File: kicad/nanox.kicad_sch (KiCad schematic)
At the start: 137 parts, among them P1 likely an ESD protection diod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, P2 likely an ESD protection diod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, P3 likely an ESD protection diod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, P4 likely an ESD protection diod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, P5 likely an ESD protection diod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, SW1 push button, left, SW2 push button, right, X1 ?, X10 unknown, marked 1C4F, likely 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, X2 unknown, marked 2GC, X3 unknown, marked 6, X4 ?, X5 ?, X6 ?, X7 ?, X8 ?, X9 unknown, marked P8W 26, Y1 crystal, likely the 32 MHz HSE

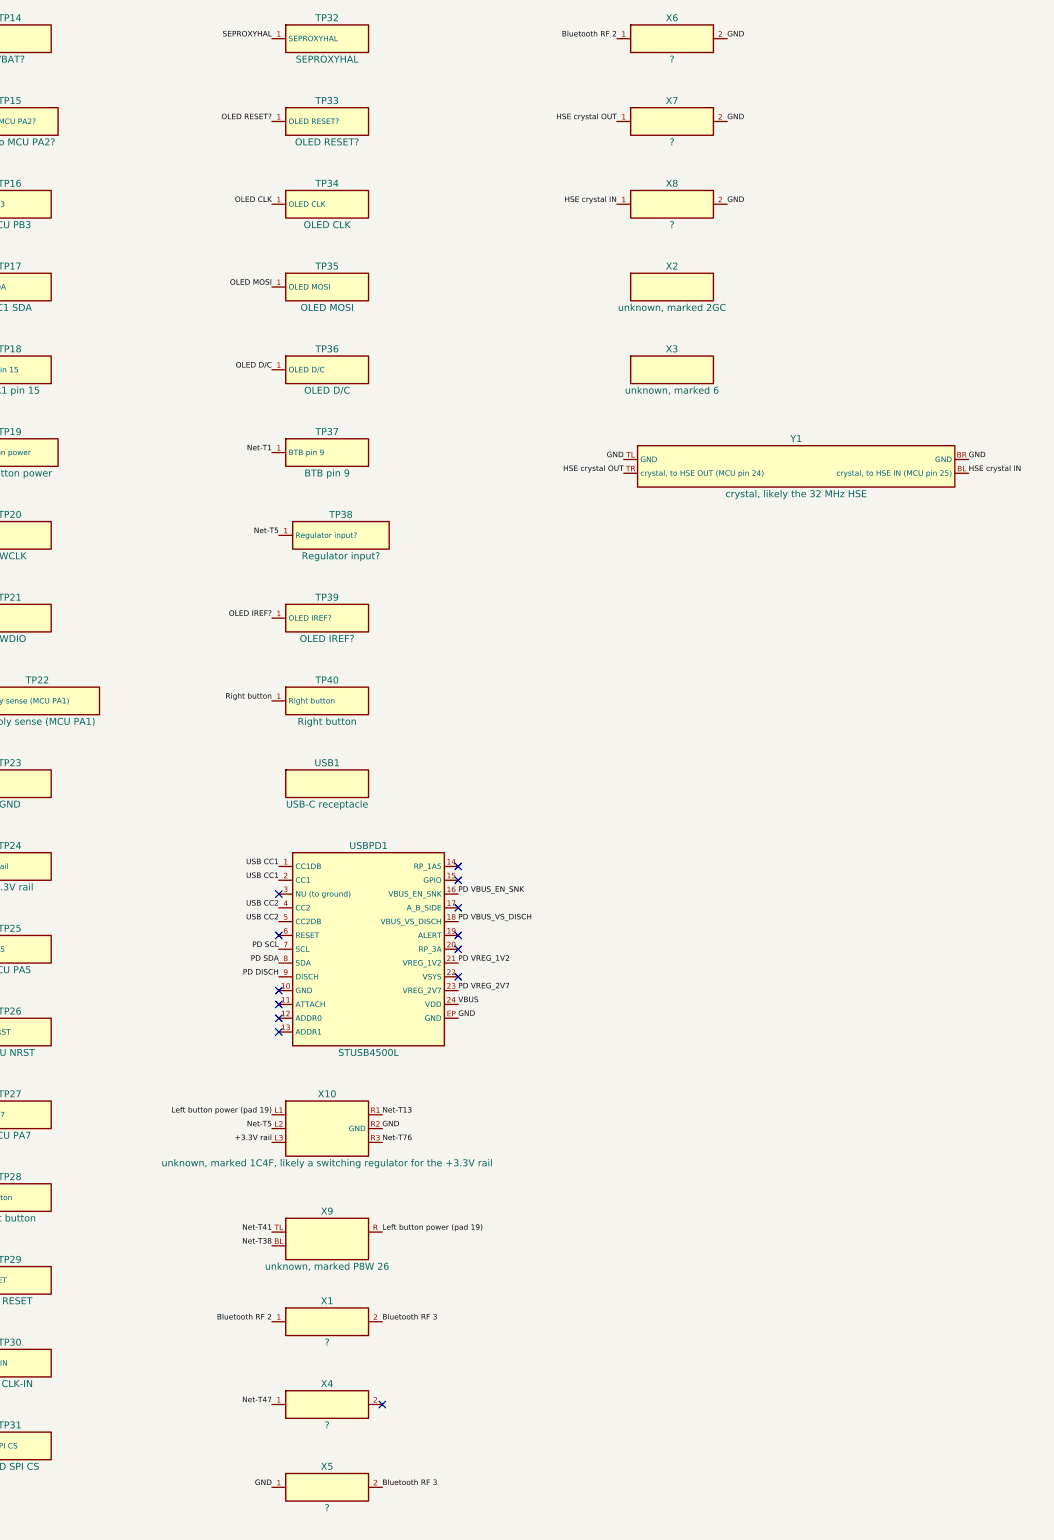
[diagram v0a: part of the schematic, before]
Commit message: Give USB1 its real pins: 24 USB-C contacts and 4 shell tabs
USB1 was a single body pad. It now has the 24 pads measured in the bare
front photo, in two staggered rows at 0.5 mm pitch (B1-B12 nearer the
mouth, A12-A1 behind), named from the USB-C pinout, plus the four shell
tabs. The traced lines land on VBUS (A4, A9, B4, B9), CC1, CC2, D+ (A6,
B6) and D- (A7, B7); the USB 3 pairs and SBU are unused. The 3D model's
solder tails now sit on the A row.

Co-Authored-By: Claude Opus 5.5 <noreply@anthropic.com>
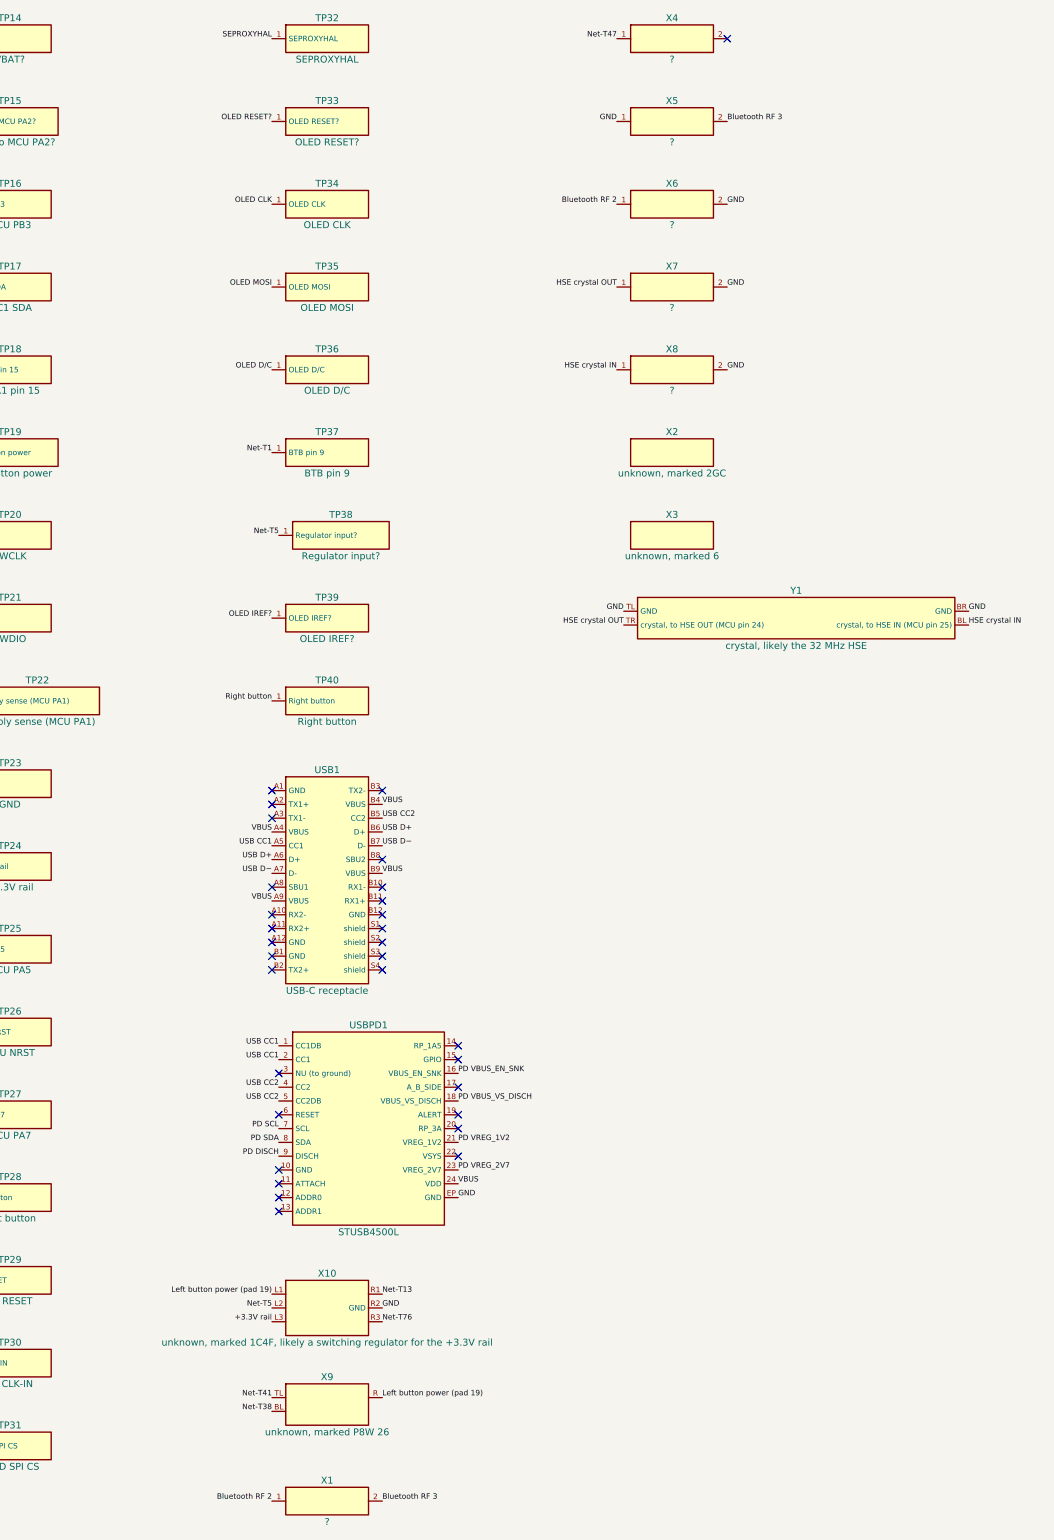
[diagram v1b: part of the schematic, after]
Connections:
- net USB CC1: now also USB1.A5 (CC1)
- net USB CC2: now also USB1.B5 (CC2)
- net USB D+: now also USB1.A6 (D+), USB1.B6 (D+)
- net USB D−: now also USB1.A7 (D-), USB1.B7 (D-)
- net VBUS: now also USB1.A4 (VBUS), USB1.A9 (VBUS), USB1.B4 (VBUS), USB1.B9 (VBUS)
- no-connect marks 61 -> 79
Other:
- moved on the sheet: USBPD1, X1, X10, X2, X3, X4, X5, X6, X7, X8, X9, Y1

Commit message: Name the display connector's power pins from the SSD1312 datasheet
The display's controller is an SSD1312, whose datasheet explains the
pins we could only guess:
- pin 12 (pad 38) is the panel's drive supply VCC, 7.5 to 16.5 V: it is
  the regulated output of X10, whose R25/R26 divider feeds it back, so
  X10 with L1 is a boost converter from the +3.3V rail, not the 3.3 V
  regulator we assumed
- pin 9 (pad 37) is likely VCOMH, which only needs C31 to ground
- pin 10 keeps IREF, set by R33 to ground; pin 6 is RES#, held low by R23
  until the MCU starts the display
Connectivity is unchanged; only names and notes.

Co-Authored-By: Claude Opus 5.5 <noreply@anthropic.com>
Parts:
- TP37: value BTB pin 9 -> OLED VCOMH?
- TP38: value Regulator input? -> OLED VCC?
- X10: value unknown, marked 1C4F, likely a switching regulator for the +3.3V rail -> unknown, marked 1C4F, likely the boost converter for the OLED panel supply
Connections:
- net Net-T1 renamed OLED VCOMH?
- net Net-T5 renamed OLED VCC?
- net Net-T76 renamed OLED VCC feedback?
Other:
- moved on the sheet: TP38
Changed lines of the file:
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@@
  (label "GND" (at 25.40 74.93 180) (effects (font (size 1.0 1.0)) (justify right bottom)))
  (label "OLED SPI CS" (at 25.40 77.47 180) (effects (font (size 1.0 1.0)) (justify right bottom)))
- (label "Net-T1" (at 25.40 80.01 180) (effects (font (size 1.0 1.0)) (justify right bottom)))
+ (label "OLED VCOMH?" (at 25.40 80.01 180) (effects (font (size 1.0 1.0)) (justify right bottom)))
  (label "OLED IREF?" (at 25.40 82.55 180) (effects (font (size 1.0 1.0)) (justify right bottom)))
  (label "+3.3V rail" (at 45.72 59.69 0) (effects (font (size 1.0 1.0)) (justify left bottom)))
- (label "Net-T5" (at 45.72 62.23 0) (effects (font (size 1.0 1.0)) (justify left bottom)))
+ (label "OLED VCC?" (at 45.72 62.23 0) (effects (font (size 1.0 1.0)) (justify left bottom)))
  (no_connect (at 45.72 64.77))
  (no_connect (at 45.72 67.31))
@@
  )
  (label "GND" (at 76.20 73.66 180) (effects (font (size 1.0 1.0)) (justify right bottom)))
- (label "Net-T5" (at 96.52 73.66 0) (effects (font (size 1.0 1.0)) (justify left bottom)))
+ (label "OLED VCC?" (at 96.52 73.66 0) (effects (font (size 1.0 1.0)) (justify left bottom)))
  (symbol (lib_id "nanox:C29") (at 86.36 88.90 0) (unit 1) (in_bom yes) (on_board yes) (dnp no)
   (property "Reference" "C29" (at 86.36 85.09 0) (effects (font (size 1.27 1.27))))
@@
  )
  (label "GND" (at 76.20 134.62 180) (effects (font (size 1.0 1.0)) (justify right bottom)))
- (label "Net-T1" (at 96.52 134.62 0) (effects (font (size 1.0 1.0)) (justify left bottom)))
+ (label "OLED VCOMH?" (at 96.52 134.62 0) (effects (font (size 1.0 1.0)) (justify left bottom)))
  (symbol (lib_id "nanox:C32") (at 86.36 149.86 0) (unit 1) (in_bom yes) (on_board yes) (dnp no)
   (property "Reference" "C32" (at 86.36 146.05 0) (effects (font (size 1.27 1.27))))
@@
   (instances (project "nanox" (path "/9fc871f3-1e36-5a01-9359-e2a20c86f96f" (reference "C33") (unit 1))))
  )
- (label "Net-T5" (at 76.20 165.10 180) (effects (font (size 1.0 1.0)) (justify right bottom)))
+ (label "OLED VCC?" (at 76.20 165.10 180) (effects (font (size 1.0 1.0)) (justify right bottom)))
  (label "GND" (at 96.52 165.10 0) (effects (font (size 1.0 1.0)) (justify left bottom)))
  (symbol (lib_id "nanox:C34") (at 86.36 180.34 0) (unit 1) (in_bom yes) (on_board yes) (dnp no)
@@
   (instances (project "nanox" (path "/9fc871f3-1e36-5a01-9359-e2a20c86f96f" (reference "C34") (unit 1))))
  )
- (label "Net-T5" (at 76.20 180.34 180) (effects (font (size 1.0 1.0)) (justify right bottom)))
+ (label "OLED VCC?" (at 76.20 180.34 180) (effects (font (size 1.0 1.0)) (justify right bottom)))
  (label "GND" (at 96.52 180.34 0) (effects (font (size 1.0 1.0)) (justify left bottom)))
  (symbol (lib_id "nanox:C35") (at 86.36 195.58 0) (unit 1) (in_bom yes) (on_board yes) (dnp no)
@@
   (instances (project "nanox" (path "/9fc871f3-1e36-5a01-9359-e2a20c86f96f" (reference "R25") (unit 1))))
  )
- (label "Net-T5" (at 185.42 256.54 180) (effects (font (size 1.0 1.0)) (justify right bottom)))
- (label "Net-T76" (at 205.74 256.54 0) (effects (font (size 1.0 1.0)) (justify left bottom)))
+ (label "OLED VCC?" (at 185.42 256.54 180) (effects (font (size 1.0 1.0)) (justify right bottom)))
+ (label "OLED VCC feedback?" (at 205.74 256.54 0) (effects (font (size 1.0 1.0)) (justify left bottom)))
  (symbol (lib_id "nanox:R26") (at 195.58 271.78 0) (unit 1) (in_bom yes) (on_board yes) (dnp no)
   (property "Reference" "R26" (at 195.58 267.97 0) (effects (font (size 1.27 1.27))))
@@
   (instances (project "nanox" (path "/9fc871f3-1e36-5a01-9359-e2a20c86f96f" (reference "R26") (unit 1))))
  )
- (label "Net-T76" (at 185.42 271.78 180) (effects (font (size 1.0 1.0)) (justify right bottom)))
+ (label "OLED VCC feedback?" (at 185.42 271.78 180) (effects (font (size 1.0 1.0)) (justify right bottom)))
  (label "GND" (at 205.74 271.78 0) (effects (font (size 1.0 1.0)) (justify left bottom)))
  (symbol (lib_id "nanox:R27") (at 195.58 287.02 0) (unit 1) (in_bom yes) (on_board yes) (dnp no)
@@
  (symbol (lib_id "nanox:TP37") (at 449.58 104.14 0) (unit 1) (in_bom yes) (on_board yes) (dnp no)
   (property "Reference" "TP37" (at 449.58 100.33 0) (effects (font (size 1.27 1.27))))
-  (property "Value" "BTB pin 9" (at 449.58 107.95 0) (effects (font (size 1.27 1.27))))
+  (property "Value" "OLED VCOMH?" (at 449.58 107.95 0) (effects (font (size 1.27 1.27))))
   (property "Footprint" "" (at 449.58 104.14 0) (effects (font (size 1.27 1.27)) hide))
   (property "Description" "test pad" (at 449.58 104.14 0) (effects (font (size 1.27 1.27)) hide))
@@
   (instances (project "nanox" (path "/9fc871f3-1e36-5a01-9359-e2a20c86f96f" (reference "TP37") (unit 1))))
  )
- (label "Net-T1" (at 439.42 104.14 180) (effects (font (size 1.0 1.0)) (justify right bottom)))
- (symbol (lib_id "nanox:TP38") (at 452.12 119.38 0) (unit 1) (in_bom yes) (on_board yes) (dnp no)
-  (property "Reference" "TP38" (at 452.12 115.57 0) (effects (font (size 1.27 1.27))))
-  (property "Value" "Regulator input?" (at 452.12 123.19 0) (effects (font (size 1.27 1.27))))
-  (property "Footprint" "" (at 452.12 119.38 0) (effects (font (size 1.27 1.27)) hide))
-  (property "Description" "test pad" (at 452.12 119.38 0) (effects (font (size 1.27 1.27)) hide))
+ (label "OLED VCOMH?" (at 439.42 104.14 180) (effects (font (size 1.0 1.0)) (justify right bottom)))
+ (symbol (lib_id "nanox:TP38") (at 449.58 119.38 0) (unit 1) (in_bom yes) (on_board yes) (dnp no)
+  (property "Reference" "TP38" (at 449.58 115.57 0) (effects (font (size 1.27 1.27))))
+  (property "Value" "OLED VCC?" (at 449.58 123.19 0) (effects (font (size 1.27 1.27))))
+  (property "Footprint" "" (at 449.58 119.38 0) (effects (font (size 1.27 1.27)) hide))
+  (property "Description" "test pad" (at 449.58 119.38 0) (effects (font (size 1.27 1.27)) hide))
   (pin "1")
   (instances (project "nanox" (path "/9fc871f3-1e36-5a01-9359-e2a20c86f96f" (reference "TP38") (unit 1))))
  )
- (label "Net-T5" (at 440.69 119.38 180) (effects (font (size 1.0 1.0)) (justify right bottom)))
+ (label "OLED VCC?" (at 439.42 119.38 180) (effects (font (size 1.0 1.0)) (justify right bottom)))
  (symbol (lib_id "nanox:TP39") (at 449.58 134.62 0) (unit 1) (in_bom yes) (on_board yes) (dnp no)
   (property "Reference" "TP39" (at 449.58 130.81 0) (effects (font (size 1.27 1.27))))
@@
  (symbol (lib_id "nanox:X10") (at 449.58 261.62 0) (unit 1) (in_bom yes) (on_board yes) (dnp no)
   (property "Reference" "X10" (at 449.58 255.27 0) (effects (font (size 1.27 1.27))))
-  (property "Value" "unknown, marked 1C4F, likely a switching regulator for the +3.3V rail" (at 449.58 267.97 0) (effects (font (size 1.27 1.27))))
+  (property "Value" "unknown, marked 1C4F, likely the boost converter for the OLED panel supply" (at 449.58 267.97 0) (effects (font (size 1.27 1.27))))
   (property "Footprint" "" (at 449.58 261.62 0) (effects (font (size 1.27 1.27)) hide))
   (property "Description" "6 terminals, SOT-23-6 style, ~1.5 x 2.7 mm body" (at 449.58 261.62 0) (effects (font (size 1.27 1.27)) hide))
@@
  )
  (label "Left button power (pad 19)" (at 439.42 259.08 180) (effects (font (size 1.0 1.0)) (justify right bottom)))
- (label "Net-T5" (at 439.42 261.62 180) (effects (font (size 1.0 1.0)) (justify right bottom)))
+ (label "OLED VCC?" (at 439.42 261.62 180) (effects (font (size 1.0 1.0)) (justify right bottom)))
  (label "+3.3V rail" (at 439.42 264.16 180) (effects (font (size 1.0 1.0)) (justify right bottom)))
  (label "Net-T13" (at 459.74 259.08 0) (effects (font (size 1.0 1.0)) (justify left bottom)))
  (label "GND" (at 459.74 261.62 0) (effects (font (size 1.0 1.0)) (justify left bottom)))
- (label "Net-T76" (at 459.74 264.16 0) (effects (font (size 1.0 1.0)) (justify left bottom)))
+ (label "OLED VCC feedback?" (at 459.74 264.16 0) (effects (font (size 1.0 1.0)) (justify left bottom)))
  (symbol (lib_id "nanox:X9") (at 449.58 279.40 0) (unit 1) (in_bom yes) (on_board yes) (dnp no)
   (property "Reference" "X9" (at 449.58 274.32 0) (effects (font (size 1.27 1.27))))
